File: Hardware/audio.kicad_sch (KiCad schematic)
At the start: 35 parts, among them J13 ANT_BNC, J14 ANT_BNC, J15 Audio IN, Q3 MMBT2222A, U10 Si4732, U9 LM358, X1 Q13FC1350000400

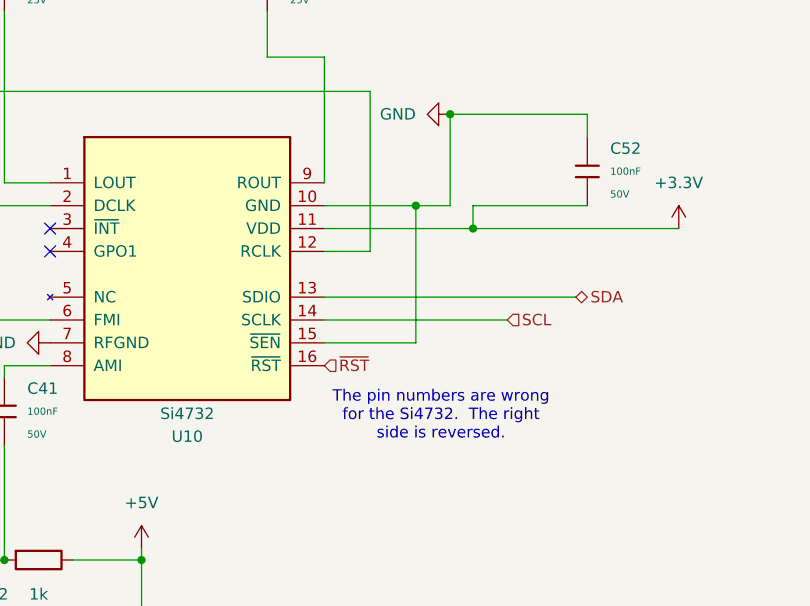
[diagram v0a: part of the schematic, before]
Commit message: Si4732 Schematic and PCB revision
Modified schematic and PCB of Si4732 chip to correct the order of pins 9-16.
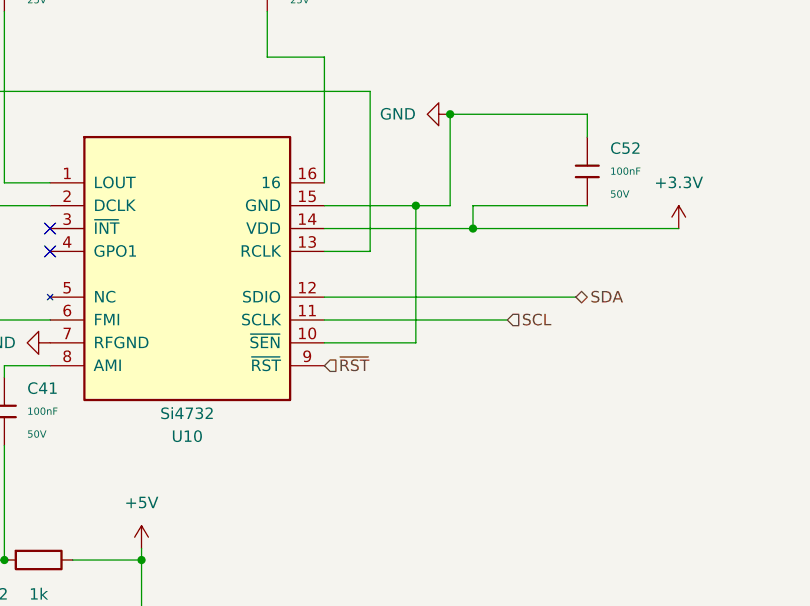
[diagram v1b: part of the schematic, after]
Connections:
- net +3.3V: now also U10.14 (VDD); no longer U10.11 (VDD)
- net SCL: now also U10.11 (SCLK); no longer U10.14 (SCLK)
- net SDA: now also U10.12 (SDIO); no longer U10.13 (SDIO)
- net ~{RST}: now also U10.9 (~{RST}); no longer U10.16 (~{RST})
- net at C36.2, X1.2: now also U10.13 (RCLK); no longer U10.12 (RCLK)
- net at C45.2: now also U10.16; no longer U10.9 (ROUT)
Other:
- note removed: "The pin numbers are wrong for the Si4732. The right side is reversed."
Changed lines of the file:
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@@
 	(generator_version "9.0")
 	(paper "A4")
-	(text "The pin numbers are wrong\nfor the Si4732.  The right\nside is reversed."
-		(exclude_from_sim no)
-		(at 119.634 133.858 0)
-		(effects
-			(font
-				(face "KiCad Font")
-				(size 1.27 1.27)
-			)
-		)
-	)
 	(junction
 		(at 121.92 62.23)
@@
 		(pin "11"
 		)
-		(pin "9"
-		)
 		(pin "16"
 		)
+		(pin "9"
+		)
 		(pin "3"
